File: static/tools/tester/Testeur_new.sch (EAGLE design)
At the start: 28 parts, among them IC1 MEGA8-P, SW1 CI-11

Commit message: [tester] add VCC pin for UART
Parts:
- removed UART: (no value), con-lstb:MA03-1
- added SV1: (no value), con-lstb:MA04-1
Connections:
- net GND: now also SV1.3; no longer UART.3
- net N$21: now also SV1.1; no longer UART.1
- net N$22: now also SV1.2; no longer UART.2
- net VCC: now also SV1.4
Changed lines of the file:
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@@
 <?xml version="1.0" encoding="utf-8"?>
 <!DOCTYPE eagle SYSTEM "eagle.dtd">
-<eagle version="6.1">
+<eagle version="6.3">
 <drawing>
 <settings>
@@
 <part name="POTAR-CONTRASTE" library="con-lstb" deviceset="MA03-1" device=""/>
 <part name="CODER-MOTOR" library="con-lstb" deviceset="MA04-1" device=""/>
-<part name="UART" library="con-lstb" deviceset="MA03-1" device=""/>
 <part name="I²C" library="con-lstb" deviceset="MA04-1" device=""/>
 <part name="ALIM" library="con-lstb" deviceset="MA03-1" device=""/>
@@
 <part name="LED2" library="led" deviceset="LED" device="3MM"/>
 <part name="SW1" library="piher" deviceset="CI-11" device=""/>
+<part name="SV1" library="con-lstb" deviceset="MA04-1" device=""/>
 </parts>
 <sheets>
@@
 <instance part="POTAR-CONTRASTE" gate="G$1" x="180.34" y="5.08"/>
 <instance part="CODER-MOTOR" gate="1" x="205.74" y="63.5" rot="R180"/>
-<instance part="UART" gate="G$1" x="208.28" y="83.82" rot="R180"/>
 <instance part="I²C" gate="1" x="167.64" y="83.82" rot="R180"/>
 <instance part="ALIM" gate="G$1" x="17.78" y="86.36"/>
@@
 <instance part="LED1" gate="G$1" x="172.72" y="137.16" rot="MR270"/>
 <instance part="LED2" gate="G$1" x="172.72" y="121.92" rot="MR270"/>
+<instance part="SV1" gate="1" x="208.28" y="81.28" rot="R180"/>
 </instances>
 <busses>
@@
 <label x="91.44" y="55.88" size="1.778" layer="95"/>
 </segment>
+<segment>
+<pinref part="SV1" gate="1" pin="4"/>
+<wire x1="200.66" y1="78.74" x2="195.58" y2="78.74" width="0.1524" layer="91"/>
+<label x="193.04" y="78.74" size="1.778" layer="95"/>
+</segment>
 </net>
 <net name="GND" class="0">
@@
 </segment>
 <segment>
-<pinref part="UART" gate="G$1" pin="3"/>
 <wire x1="200.66" y1="81.28" x2="195.58" y2="81.28" width="0.1524" layer="91"/>
 <label x="193.04" y="81.28" size="1.778" layer="95"/>
+<pinref part="SV1" gate="1" pin="3"/>
 </segment>
 <segment>
@@
 <wire x1="142.24" y1="68.58" x2="149.86" y2="68.58" width="0.1524" layer="91"/>
 <wire x1="149.86" y1="68.58" x2="177.8" y2="81.28" width="0.1524" layer="91"/>
-<pinref part="UART" gate="G$1" pin="1"/>
 <wire x1="177.8" y1="81.28" x2="190.5" y2="86.36" width="0.1524" layer="91"/>
 <wire x1="190.5" y1="86.36" x2="200.66" y2="86.36" width="0.1524" layer="91"/>
+<pinref part="SV1" gate="1" pin="1"/>
 </segment>
 </net>
 <net name="N$22" class="0">
 <segment>
-<pinref part="UART" gate="G$1" pin="2"/>
 <wire x1="200.66" y1="83.82" x2="190.5" y2="83.82" width="0.1524" layer="91"/>
 <wire x1="190.5" y1="83.82" x2="177.8" y2="78.74" width="0.1524" layer="91"/>
@@
 <pinref part="IC1" gate="G$1" pin="PD1(TXD)"/>
 <wire x1="149.86" y1="66.04" x2="142.24" y2="66.04" width="0.1524" layer="91"/>
-</segment>
-</net>
+<pinref part="SV1" gate="1" pin="2"/>
+</segment>
+</net>

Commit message: [tester] create ihm board
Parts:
- removed CODEUR-IHM, I²C-IHM: (no value), con-lstb:MA04-1
- removed SERVO/PWM-IHM: (no value), con-lstb:MA03-1
- removed SW1: CI-11, piher:CI-11
- added CODER-IHM, I2C-IHM: (no value), con-lstb:MA04-1
- added ENCODER-IHM: CI-11, piher:CI-11
- added LCD1-IHM, LCD2-IHM: (no value), con-lstb:MA08-1
- added SERVO-IHM: (no value), con-lstb:MA03-1
- UART-IHM: device con-lstb:MA03-1 -> con-lstb:MA04-1
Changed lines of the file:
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@@
 <?xml version="1.0" encoding="utf-8"?>
 <!DOCTYPE eagle SYSTEM "eagle.dtd">
-<eagle version="6.3">
+<eagle version="6.1">
 <drawing>
 <settings>
@@
 <part name="I²C" library="con-lstb" deviceset="MA04-1" device=""/>
 <part name="ALIM" library="con-lstb" deviceset="MA03-1" device=""/>
-<part name="SERVO/PWM-IHM" library="con-lstb" deviceset="MA03-1" device=""/>
-<part name="UART-IHM" library="con-lstb" deviceset="MA03-1" device=""/>
-<part name="I²C-IHM" library="con-lstb" deviceset="MA04-1" device=""/>
-<part name="CODEUR-IHM" library="con-lstb" deviceset="MA04-1" device=""/>
 <part name="R3" library="resistor" deviceset="R-EU_" device="0204/5"/>
 <part name="R4" library="resistor" deviceset="R-EU_" device="0204/5"/>
 <part name="LED1" library="led" deviceset="LED" device="3MM"/>
 <part name="LED2" library="led" deviceset="LED" device="3MM"/>
-<part name="SW1" library="piher" deviceset="CI-11" device=""/>
 <part name="SV1" library="con-lstb" deviceset="MA04-1" device=""/>
+<part name="SERVO-IHM" library="con-lstb" deviceset="MA03-1" device=""/>
+<part name="CODER-IHM" library="con-lstb" deviceset="MA04-1" device=""/>
+<part name="UART-IHM" library="con-lstb" deviceset="MA04-1" device=""/>
+<part name="I2C-IHM" library="con-lstb" deviceset="MA04-1" device=""/>
+<part name="ENCODER-IHM" library="piher" deviceset="CI-11" device=""/>
+<part name="LCD1-IHM" library="con-lstb" deviceset="MA08-1" device=""/>
+<part name="LCD2-IHM" library="con-lstb" deviceset="MA08-1" device=""/>
 </parts>
 <sheets>
@@
 </plain>
 <instances>
-<instance part="SERVO/PWM-IHM" gate="G$1" x="10.16" y="76.2"/>
-<instance part="UART-IHM" gate="G$1" x="73.66" y="76.2"/>
-<instance part="I²C-IHM" gate="1" x="38.1" y="76.2"/>
-<instance part="CODEUR-IHM" gate="1" x="53.34" y="76.2"/>
-<instance part="SW1" gate="A" x="15.24" y="55.88"/>
-<instance part="SW1" gate="B" x="33.02" y="55.88"/>
+<instance part="SERVO-IHM" gate="G$1" x="71.12" y="63.5"/>
+<instance part="CODER-IHM" gate="1" x="55.88" y="66.04"/>
+<instance part="UART-IHM" gate="1" x="38.1" y="66.04"/>
+<instance part="I2C-IHM" gate="1" x="12.7" y="68.58"/>
+<instance part="ENCODER-IHM" gate="A" x="76.2" y="40.64"/>
+<instance part="ENCODER-IHM" gate="B" x="93.98" y="40.64"/>
+<instance part="LCD1-IHM" gate="1" x="7.62" y="33.02"/>
+<instance part="LCD2-IHM" gate="1" x="27.94" y="33.02"/>
 </instances>
 <busses>

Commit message: [tester] modify to V2 Alpha.
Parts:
- removed CODER-MOTOR, I²C, SV1: (no value), con-lstb:MA04-1
- removed ENCODER-SELECT, LCD-GND: (no value), con-lstb:MA05-1
- removed LCD-CONTRASTE, POTAR-CONTRASTE, RETURN, SERVO/PWM: (no value), con-lstb:MA03-1
- removed LCD-DATA: (no value), con-lstb:MA06-1
- removed LCD1-IHM, LCD2-IHM: (no value), con-lstb:MA08-1
- added AR, RETURN_IHM: (no value), pinhead:PINHD-1X2
- added C1-REGULATOR1, C2-REGULATOR1: (no value), capacitor-wima:C5/5
- added IC3: (no value), v-reg:78XXS
- added JP1, JP2: (no value), pinhead:PINHD-2X12
- added JP3: (no value), pinhead:PINHD-1X16
- added MOTOR, X1: (no value), con-wago-500:W237-102
- added POTAR, SERVO-IHM2: (no value), con-lstb:MA03-1
- added Q2: MFR475V, transistor-power:MFR475V
- added R2: (no value), resistor:R-EU_0204/7
- ALIM: device con-lstb:MA03-1 -> pinhead:PINHD-1X2
- LED1, LED2: device led:LED3MM -> led:LED5MM
- R1: device rcl:R-EU_0204/5 -> rcl:R-EU_0204/7
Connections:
- net N$25 renamed LED1
- net N$26 renamed LED2
- removed net N$5: CODER-MOTOR.2, IC1.PD3(INT1)
- new net 5V_POWER: C2-REGULATOR1.1, IC3.OUT, SERVO-IHM.2, SERVO-IHM2.2
- new net 5V_POW_IHM: JP2.3
- new net ALIM_EXT: C1-REGULATOR1.1, IC3.IN, MOTOR-1.KL, X1-1.KL
- new net ENCODER1: IC1.PD4(XCK/T0), JP1.24
- new net ENCODER2: IC1.PD5(T1), JP1.23
- new net GND_IHM: AR.1, C1-REGULATOR1.2, C2-REGULATOR1.2, CODER-IHM.2, ENCODER-IHMA.C, ENCODER-IHMB.D, I2C-IHM.2, IC3.GND, JP2.1, JP3.1, JP3.10, JP3.5, JP3.7, JP3.8, JP3.9, LED1.C, LED2.C, POTAR.3, Q2.E, RETURN_IHM.1, SERVO-IHM.1, SERVO-IHM2.1, UART-IHM.2, X1-2.KL
- new net INT_ODO1: IC1.PD2(INT0), JP1.18
- new net LCD1: IC1.PD7(AIN1), JP1.19
- new net LCD2: IC1.PB0(ICP), JP1.17
- new net LCD3: IC1.PB1(OC1A), JP1.15
- new net LCD5: IC1.PB4(MISO), JP1.9
- new net LCD6: IC1.PB5(SCK), JP1.7
- new net N$25: JP2.19, JP3.4
- new net N$26: JP2.17, JP3.6
- new net N$34: JP2.7, JP3.14
- new net N$35: JP2.11, R2.1, SERVO-IHM.3
- new net N$36: JP2.8, RETURN_IHM.2
- new net N$37: AR.2, JP2.2
- new net N$39: JP3.3, POTAR.1
- new net N$40: MOTOR-2.KL, Q2.C
- new net RETURN: IC1.PC3(ADC3), JP1.8
- new net RX: IC1.PD0(RXD), JP1.14
- new net SCL: IC1.PC5(ADC5/SCL), JP1.12
- new net SDA: IC1.PC4(ADC4/SDA), JP1.10
- new net SELECT: IC1.PD6(AIN0), JP1.21
- new net SENS_ODO+SERVO2: IC1.PD3(INT1), JP1.22
- new net SERVO/PWM: IC1.PB3(MOSI/OC2), JP1.11
- new net TX: IC1.PD1(TXD), JP1.16
- new net VCC_IHM: CODER-IHM.1, I2C-IHM.1, JP2.5, JP3.2, POTAR.2, UART-IHM.1
- net GND: now also JP1.1; no longer CODER-MOTOR.4, ENCODER-SELECT.4, ENCODER-SELECT.5, I²C.2, LCD-CONTRASTE.3, LCD-GND.1, LCD-GND.2, LCD-GND.3, LCD-GND.4, LCD-GND.5, LED1.C, LED2.C, POTAR-CONTRASTE.3, RETURN.3, SERVO/PWM.3, SV1.3
- net N$10: now also I2C-IHM.3, JP2.10; no longer IC1.PB0(ICP), LCD-DATA.2
- net N$11: now also I2C-IHM.4, JP2.12; no longer IC1.PB3(MOSI/OC2), SERVO/PWM.1
- net N$12: now also JP2.4, LED1.A; no longer IC1.PB5(SCK), LCD-DATA.6
- net N$13: now also JP2.6, LED2.A; no longer IC1.PD7(AIN1), LCD-DATA.1
- net N$14: now also JP2.14, UART-IHM.3; no longer IC1.PB1(OC1A), LCD-DATA.3
- net N$15: now also JP2.16, UART-IHM.4; no longer IC1.PB2(SS/OC1B), LCD-DATA.4
- net N$16: now also CODER-IHM.3, JP2.18; no longer IC1.PB4(MISO), LCD-DATA.5
- net N$17: now also CODER-IHM.4, JP2.22, SERVO-IHM2.3; no longer CODER-MOTOR.1, IC1.PD2(INT0)
- net N$18: now also ENCODER-IHMA.A, JP2.24; no longer LED2.A, R3.2
- net N$21: now also ENCODER-IHMA.B, JP2.23; no longer IC1.PD0(RXD), SV1.1
- net N$22: now also ENCODER-IHMB.E, JP2.21; no longer IC1.PD1(TXD), SV1.2
- net N$27: now also JP2.15, JP3.11; no longer IC1.PC3(ADC3), RETURN.1
- net N$28: now also JP1.4; no longer LED1.A
- net N$29: now also JP2.13, JP3.12; no longer IC1.PC4(ADC4/SDA), I²C.3
- net N$3: now also IC1.PC0(ADC0), JP1.2; no longer LCD-CONTRASTE.1, POTAR-CONTRASTE.1
- net N$30: now also JP2.9, JP3.13; no longer IC1.PC5(ADC5/SCL), I²C.4
- net N$6: now also ALIM.2; no longer ALIM.3
- net N$7: now also JP1.6, R3.2; no longer ENCODER-SELECT.1, IC1.PD4(XCK/T0)
- net N$8: now also Q2.B, R2.2; no longer ENCODER-SELECT.2, IC1.PD5(T1)
- net N$9: now also IC1.PB2(SS/OC1B), JP1.13; no longer ENCODER-SELECT.3, IC1.PD6(AIN0)
- net VCC: now also JP1.5; no longer CODER-MOTOR.3, I²C.1, LCD-CONTRASTE.2, POTAR-CONTRASTE.2, SERVO/PWM.2, SV1.4
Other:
- moved on the sheet: CODER-IHM, ENCODER-IHMA, ENCODER-IHMB, I2C-IHM, R3, R4, SERVO-IHM, UART-IHM

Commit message: [tester] improve V2.
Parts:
- removed UART-IHM: (no value), con-lstb:MA04-1
- added SERVO-IHM1: (no value), con-lstb:MA03-1
- added SWITCH_5V: (no value), pinhead:PINHD-1X3
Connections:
- removed net N$15: JP2.16, UART-IHM.4
- new net 5V_P/A: SERVO-IHM.2, SERVO-IHM1.2, SERVO-IHM2.2, SWITCH_5V.2
- new net N$42: JP2.16, SERVO-IHM2.3
- net 5V_POWER: now also SWITCH_5V.3; no longer SERVO-IHM.2, SERVO-IHM2.2
- net GND_IHM: now also ENCODER-IHMA.B, SERVO-IHM1.1; no longer ENCODER-IHMA.C, UART-IHM.2
- net N$14: now also SERVO-IHM1.3; no longer UART-IHM.3
- net N$17: no longer SERVO-IHM2.3
- net N$21: now also ENCODER-IHMA.C; no longer ENCODER-IHMA.B
- net VCC_IHM: now also SWITCH_5V.1; no longer UART-IHM.1
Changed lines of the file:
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@@
 <part name="SERVO-IHM" library="con-lstb" deviceset="MA03-1" device=""/>
 <part name="CODER-IHM" library="con-lstb" deviceset="MA04-1" device=""/>
-<part name="UART-IHM" library="con-lstb" deviceset="MA04-1" device=""/>
 <part name="I2C-IHM" library="con-lstb" deviceset="MA04-1" device=""/>
 <part name="ENCODER-IHM" library="piher" deviceset="CI-11" device=""/>
@@
 <part name="R2" library="resistor" deviceset="R-EU_" device="0204/7"/>
 <part name="X1" library="con-wago-500" deviceset="W237-102" device=""/>
+<part name="SERVO-IHM1" library="con-lstb" deviceset="MA03-1" device="">
+<attribute name="MF" value=""/>
+<attribute name="MPN" value=""/>
+<attribute name="OC_FARNELL" value="unknown"/>
+<attribute name="OC_NEWARK" value="unknown"/>
+</part>
+<part name="SWITCH_5V" library="pinhead" deviceset="PINHD-1X3" device=""/>
 </parts>
 <sheets>
@@
 <instance part="X1" gate="-1" x="5.08" y="33.02"/>
 <instance part="X1" gate="-2" x="5.08" y="27.94"/>
+<instance part="SWITCH_5V" gate="A" x="81.28" y="35.56"/>
 </instances>
 <busses>
@@
 <pinref part="C2-REGULATOR1" gate="G$1" pin="1"/>
 <wire x1="40.64" y1="38.1" x2="40.64" y2="35.56" width="0.1524" layer="91"/>
-<wire x1="40.64" y1="38.1" x2="43.18" y2="38.1" width="0.1524" layer="91"/>
 <junction x="40.64" y="38.1"/>
 <label x="43.18" y="38.1" size="1.778" layer="95"/>
+<wire x1="40.64" y1="38.1" x2="60.96" y2="38.1" width="0.1524" layer="91"/>
+<wire x1="60.96" y1="38.1" x2="66.04" y2="33.02" width="0.1524" layer="91"/>
+<pinref part="SWITCH_5V" gate="A" pin="3"/>
+<wire x1="66.04" y1="33.02" x2="78.74" y2="33.02" width="0.1524" layer="91"/>
 </segment>
 </net>
@@
 </segment>
 </net>
+<net name="5V_P/A" class="0">
+<segment>
+<pinref part="SWITCH_5V" gate="A" pin="2"/>
+<wire x1="78.74" y1="35.56" x2="68.58" y2="35.56" width="0.1524" layer="91"/>
+<label x="66.04" y="35.56" size="1.778" layer="95"/>
+</segment>
+</net>
+<net name="VCC_IHM" class="0">
+<segment>
+<pinref part="SWITCH_5V" gate="A" pin="1"/>
+<wire x1="71.12" y1="38.1" x2="78.74" y2="38.1" width="0.1524" layer="91"/>
+<label x="66.04" y="38.1" size="1.778" layer="95"/>
+</segment>
+</net>
 </nets>
 </sheet>
@@
 <instance part="SERVO-IHM" gate="G$1" x="53.34" y="48.26" rot="R180"/>
 <instance part="CODER-IHM" gate="1" x="213.36" y="2.54" rot="R180"/>
-<instance part="UART-IHM" gate="1" x="172.72" y="7.62" rot="R180"/>
 <instance part="I2C-IHM" gate="1" x="147.32" y="12.7" rot="R180"/>
 <instance part="ENCODER-IHM" gate="A" x="104.14" y="-7.62" rot="R270"/>
@@
 <instance part="MOTOR" gate="-2" x="78.74" y="60.96"/>
 <instance part="R2" gate="G$1" x="66.04" y="48.26"/>
+<instance part="SERVO-IHM1" gate="G$1" x="172.72" y="10.16" rot="R180"/>
 </instances>
 <busses>
@@
 </segment>
 <segment>
-<pinref part="UART-IHM" gate="1" pin="2"/>
-<wire x1="165.1" y1="10.16" x2="157.48" y2="10.16" width="0.1524" layer="91"/>
-<label x="157.48" y="10.16" size="1.778" layer="95"/>
+<wire x1="165.1" y1="12.7" x2="154.94" y2="12.7" width="0.1524" layer="91"/>
+<label x="154.94" y="12.7" size="1.778" layer="95"/>
+<pinref part="SERVO-IHM1" gate="G$1" pin="1"/>
 </segment>
 <segment>
@@
 <wire x1="205.74" y1="5.08" x2="198.12" y2="5.08" width="0.1524" layer="91"/>
 <label x="195.58" y="5.08" size="1.778" layer="95"/>
-</segment>
-<segment>
-<pinref part="ENCODER-IHM" gate="A" pin="C"/>
-<wire x1="111.76" y1="-7.62" x2="116.84" y2="-7.62" width="0.1524" layer="91"/>
-<label x="114.3" y="-7.62" size="1.778" layer="95"/>
 </segment>
 <segment>
@@
 <label x="78.74" y="38.1" size="1.778" layer="95"/>
 </segment>
+<segment>
+<pinref part="ENCODER-IHM" gate="A" pin="B"/>
+<wire x1="99.06" y1="-10.16" x2="93.98" y2="-10.16" width="0.1524" layer="91"/>
+<label x="91.44" y="-10.16" size="1.778" layer="95"/>
+</segment>
 </net>
 <net name="N$10" class="0">
@@
 <wire x1="68.58" y1="17.78" x2="55.88" y2="17.78" width="0.1524" layer="91"/>
 <label x="53.34" y="17.78" size="1.778" layer="95"/>
-</segment>
-<segment>
-<pinref part="UART-IHM" gate="1" pin="1"/>
-<wire x1="165.1" y1="12.7" x2="157.48" y2="12.7" width="0.1524" layer="91"/>
-<label x="157.48" y="12.7" size="1.778" layer="95"/>
 </segment>
 <segment>
@@
 <segment>
 <pinref part="JP2" gate="A" pin="14"/>
-<pinref part="UART-IHM" gate="1" pin="3"/>
 <wire x1="76.2" y1="7.62" x2="165.1" y2="7.62" width="0.1524" layer="91"/>
-</segment>
-</net>
-<net name="N$15" class="0">
-<segment>
-<pinref part="UART-IHM" gate="1" pin="4"/>
-<pinref part="JP2" gate="A" pin="16"/>
-<wire x1="165.1" y1="5.08" x2="76.2" y2="5.08" width="0.1524" layer="91"/>
+<pinref part="SERVO-IHM1" gate="G$1" pin="3"/>
 </segment>
 </net>
@@
 <pinref part="CODER-IHM" gate="1" pin="4"/>
 <wire x1="147.32" y1="0" x2="205.74" y2="0" width="0.1524" layer="91"/>
-<pinref part="SERVO-IHM2" gate="G$1" pin="3"/>
-<wire x1="167.64" y1="-20.32" x2="149.86" y2="-20.32" width="0.1524" layer="91"/>
-<wire x1="149.86" y1="-20.32" x2="147.32" y2="-17.78" width="0.1524" layer="91"/>
-<wire x1="147.32" y1="-17.78" x2="147.32" y2="-5.08" width="0.1524" layer="91"/>
-<wire x1="147.32" y1="-5.08" x2="144.78" y2="-2.54" width="0.1524" layer="91"/>
-<junction x="144.78" y="-2.54"/>
 </segment>
 </net>
@@
 <net name="N$21" class="0">
 <segment>
-<pinref part="ENCODER-IHM" gate="A" pin="B"/>
-<wire x1="99.06" y1="-10.16" x2="66.04" y2="-10.16" width="0.1524" layer="91"/>
-<wire x1="66.04" y1="-10.16" x2="63.5" y2="-7.62" width="0.1524" layer="91"/>
 <wire x1="63.5" y1="-7.62" x2="63.5" y2="-5.08" width="0.1524" layer="91"/>
 <pinref part="JP2" gate="A" pin="23"/>
 <wire x1="63.5" y1="-5.08" x2="68.58" y2="-5.08" width="0.1524" layer="91"/>
+<wire x1="63.5" y1="-7.62" x2="71.12" y2="-15.24" width="0.1524" layer="91"/>
+<wire x1="71.12" y1="-15.24" x2="106.68" y2="-15.24" width="0.1524" layer="91"/>
+<wire x1="106.68" y1="-15.24" x2="111.76" y2="-10.16" width="0.1524" layer="91"/>
+<pinref part="ENCODER-IHM" gate="A" pin="C"/>
+<wire x1="111.76" y1="-10.16" x2="111.76" y2="-7.62" width="0.1524" layer="91"/>
 </segment>
 </net>
@@
 </segment>
 </net>
-<net name="5V_POWER" class="0">
-<segment>
-<pinref part="SERVO-IHM" gate="G$1" pin="2"/>
-<wire x1="45.72" y1="48.26" x2="38.1" y2="48.26" width="0.1524" layer="91"/>
-<label x="30.48" y="48.26" size="1.778" layer="95"/>
-</segment>
-<segment>
-<pinref part="SERVO-IHM2" gate="G$1" pin="2"/>
-<wire x1="167.64" y1="-17.78" x2="160.02" y2="-17.78" width="0.1524" layer="91"/>
-<label x="152.4" y="-17.78" size="1.778" layer="95"/>
-</segment>
-</net>
 <net name="N$8" class="0">
 <segment>
@@
 </segment>
 </net>
+<net name="N$42" class="0">
+<segment>
+<pinref part="SERVO-IHM2" gate="G$1" pin="3"/>
+<wire x1="167.64" y1="-20.32" x2="149.86" y2="-20.32" width="0.1524" layer="91"/>
+<wire x1="149.86" y1="-20.32" x2="147.32" y2="-17.78" width="0.1524" layer="91"/>
+<pinref part="JP2" gate="A" pin="16"/>
+<wire x1="127" y1="5.08" x2="76.2" y2="5.08" width="0.1524" layer="91"/>
+<wire x1="147.32" y1="-17.78" x2="147.32" y2="-15.24" width="0.1524" layer="91"/>
+<wire x1="147.32" y1="-15.24" x2="127" y2="5.08" width="0.1524" layer="91"/>
+</segment>
+</net>
+<net name="5V_P/A" class="0">
+<segment>
+<pinref part="SERVO-IHM" gate="G$1" pin="2"/>
+<wire x1="45.72" y1="48.26" x2="38.1" y2="48.26" width="0.1524" layer="91"/>
+<label x="30.48" y="48.26" size="1.778" layer="95"/>
+</segment>
+<segment>
+<pinref part="SERVO-IHM2" gate="G$1" pin="2"/>
+<wire x1="167.64" y1="-17.78" x2="160.02" y2="-17.78" width="0.1524" layer="91"/>
+<label x="152.4" y="-17.78" size="1.778" layer="95"/>
+</segment>
+<segment>
+<pinref part="SERVO-IHM1" gate="G$1" pin="2"/>
+<wire x1="165.1" y1="10.16" x2="154.94" y2="10.16" width="0.1524" layer="91"/>
+<label x="154.94" y="10.16" size="1.778" layer="95"/>
+</segment>
+</net>

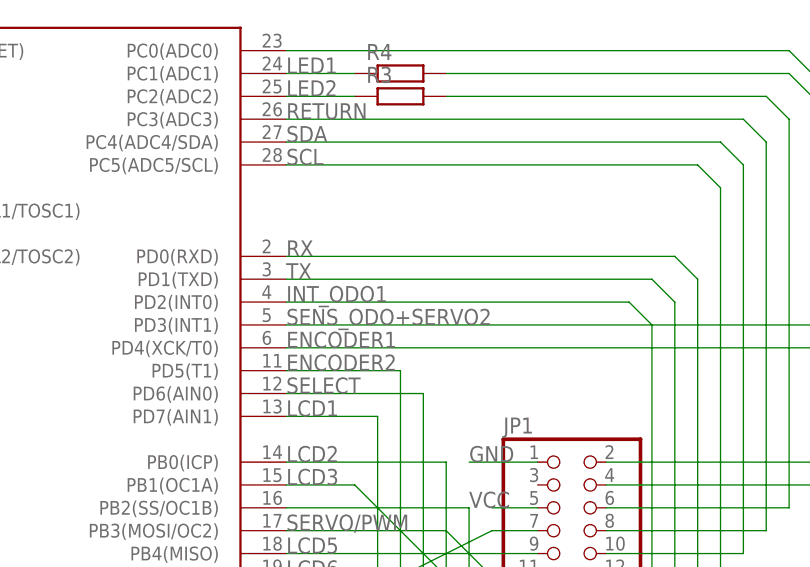
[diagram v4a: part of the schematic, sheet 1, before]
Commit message: [tester] add pins correspondance.
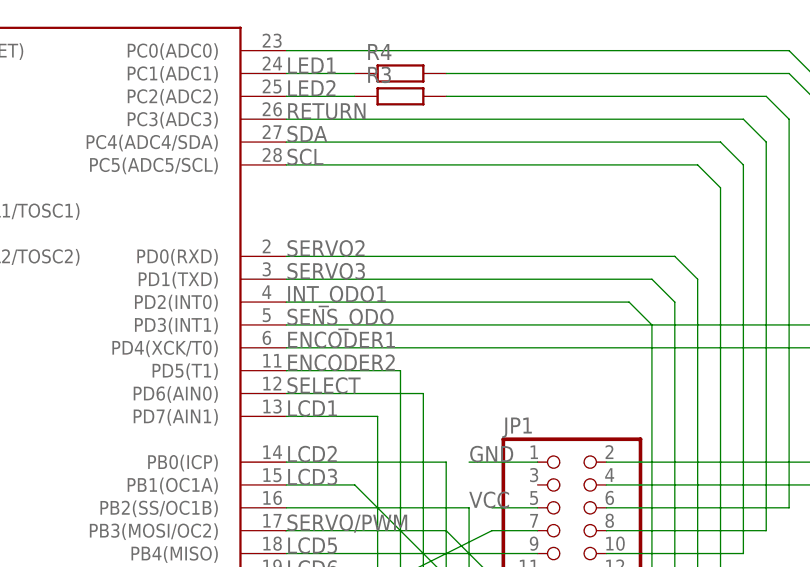
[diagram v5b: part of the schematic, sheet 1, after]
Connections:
- net RX renamed SERVO2
- net SENS_ODO+SERVO2 renamed SENS_ODO
- net TX renamed SERVO3
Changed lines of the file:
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@@
 </segment>
 </net>
-<net name="SENS_ODO+SERVO2" class="0">
+<net name="SENS_ODO" class="0">
 <segment>
 <pinref part="IC1" gate="G$1" pin="PD3(INT1)"/>
@@
 </segment>
 </net>
-<net name="TX" class="0">
+<net name="SERVO3" class="0">
 <segment>
 <pinref part="IC1" gate="G$1" pin="PD1(TXD)"/>
@@
 </segment>
 </net>
-<net name="RX" class="0">
+<net name="SERVO2" class="0">
 <segment>
 <pinref part="IC1" gate="G$1" pin="PD0(RXD)"/>
